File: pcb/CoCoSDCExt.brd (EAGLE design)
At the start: 101.6 x 47.3 mm, 59 parts, among them IC1 AM29F040J, IC10 YAC512-M, IC14 TL974, IC15 TL974, IC2 XC9572XLVQG64, IC3 AS6C4008SIN, IC4 SN76489R, IC5 16MHz, IC6 16MHz, IC9 YMF262-M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

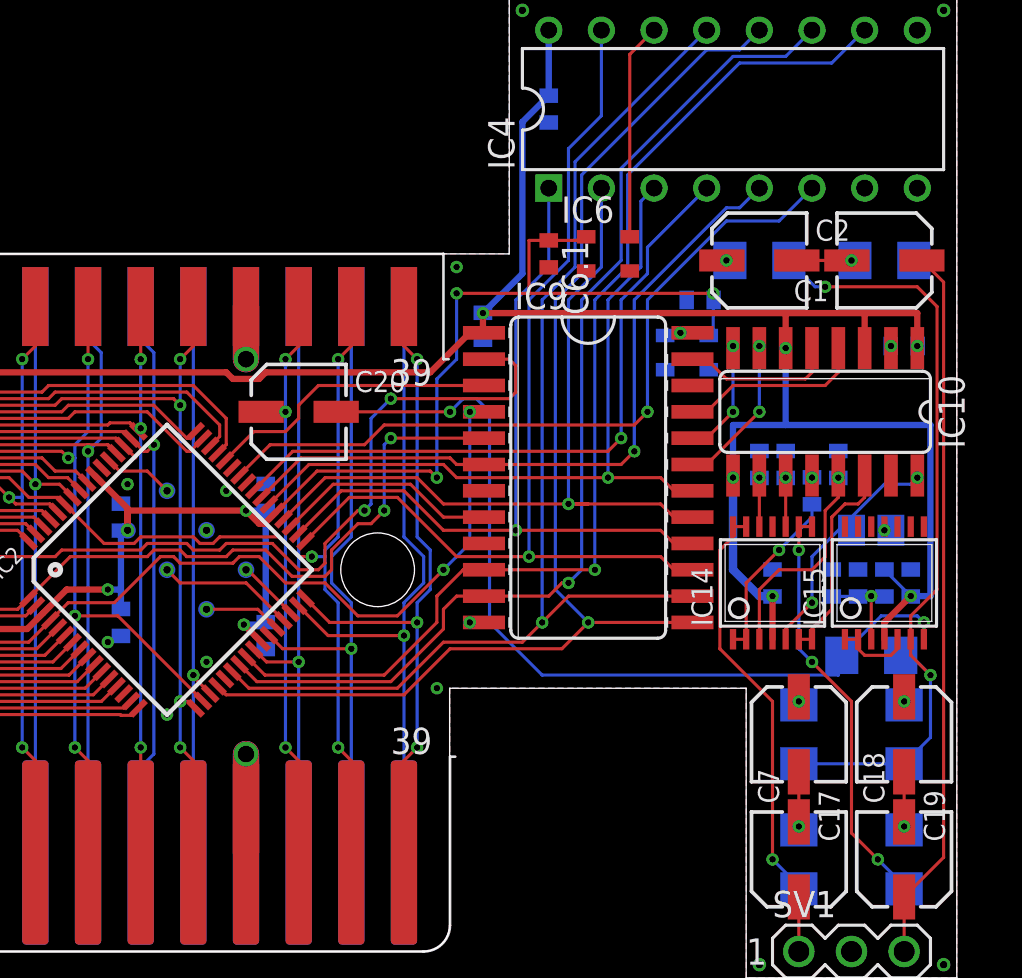
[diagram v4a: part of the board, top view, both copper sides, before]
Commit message: Fixed SN signalling
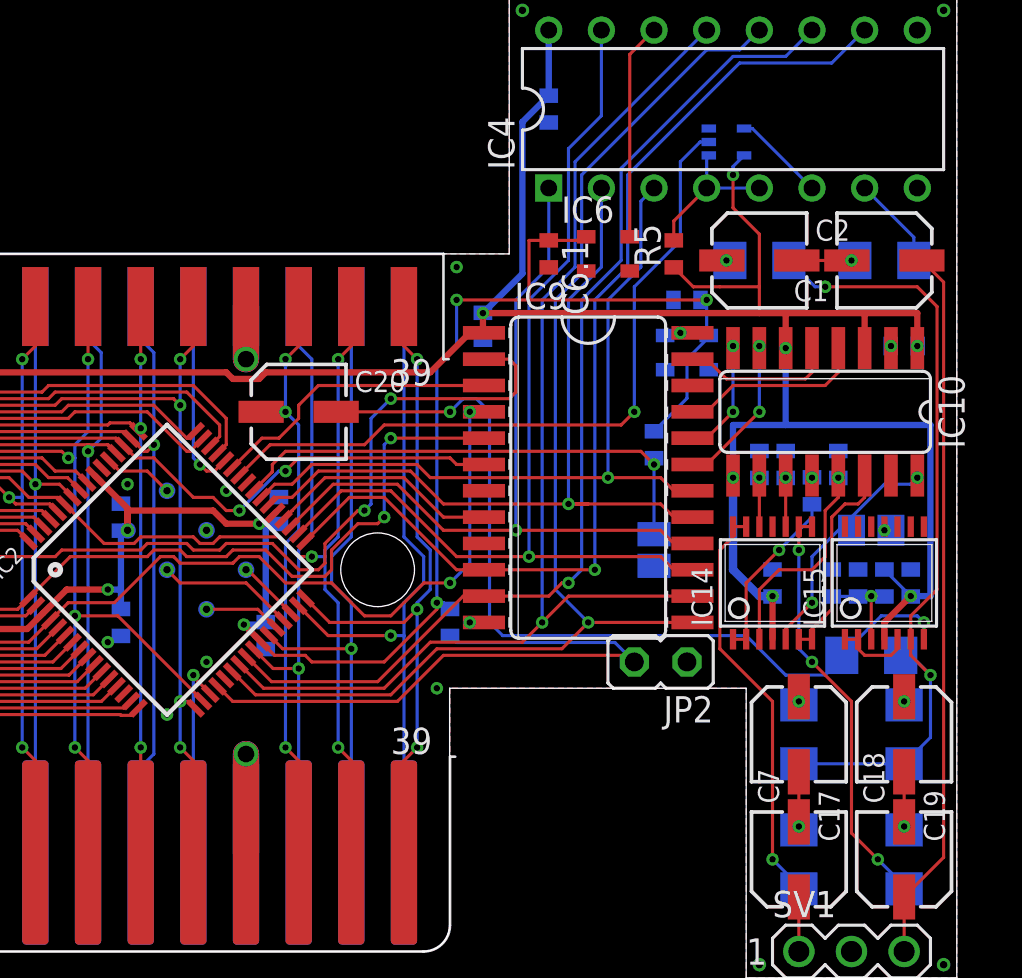
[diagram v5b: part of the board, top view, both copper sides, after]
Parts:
- added IC7: 74AHC1G08DCK, 74xx-little-us:SC70-5
- added JP2: (no value), jumper-jlb:JP1
- added R3, R4: 10K, resistor:R0402
- added R5: 2K2, resistor:R0402
- added SJ1: (no value), jumper:SJ
- IC5: value 16MHz -> 14.318MHz
- IC6: value 16MHz -> 4MHz
- moved C2.4 0.90 mm to (18.1, 21.3)
- moved C5.1 0.63 mm to (37.8, 31.4)
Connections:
- removed net !WE_AUDIO: IC2.39, IC4.5, IC9.6
- new net !CE_SN': IC4.6, IC7.4
- new net !CTS': IC2.44, X2.32
- new net N$5: IC2.40, R4.2, SJ1.2
- net !CE_SN: now also IC7.2; no longer IC4.6
- net !CE_YMF262: now also IC2.36; no longer IC2.35
- net !CTS: no longer X2.32
- net !RESET_AUDIO: now also IC2.43; no longer IC2.44
- net !WE: now also IC9.6
- net +3V3: now also R3.1, R4.1
- net +5V: now also IC7.5, R5.1
- net DB0: now also IC2.33; no longer IC2.24
- net DB1: now also IC2.24; no longer IC2.23
- net DB2: now also IC2.22; no longer IC2.20
- net DB3: now also IC2.23; no longer IC2.22
- net DB4: now also IC2.34; no longer IC2.33
- net DB5: now also IC2.35; no longer IC2.34
- net DB6: now also IC2.38; no longer IC2.36
- net DB7: now also IC2.39; no longer IC2.38
- net GND: now also IC7.3, JP2.1, SJ1.1
- net N$4: now also IC2.20, JP2.2, R3.2; no longer IC2.43
- net READY: now also IC4.5, IC7.1, R5.2; no longer IC2.40
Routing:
- net !WE_AUDIO: track 34.7 -> 0.00 mm, vias 1 -> 0
- net N$4: track 0.00 -> 30.9 mm
- net READY: track 32.5 -> 7.34 mm, vias 1 -> 0
- net N$5: track 0.00 -> 24.2 mm, vias 0 -> 1
- net !WE: track 64.0 -> 83.1 mm, vias 0 -> 2
- net !CTS: track 27.6 -> 9.79 mm
- net +3V3: track 130.6 -> 144.1 mm
- net +5V: track 237.7 -> 250.5 mm, vias 13 -> 14
- net !CTS': track 0.00 -> 9.30 mm, vias 0 -> 1
- net SN_CH_0: track 0.00 -> 4.48 mm
- net !CE_SN': track 0.00 -> 4.47 mm
- net DB0: track 54.0 -> 50.3 mm
- net !CE_SN: track 36.5 -> 35.1 mm
- net DB1: track 51.8 -> 51.0 mm
- net DB6: track 38.2 -> 38.9 mm
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
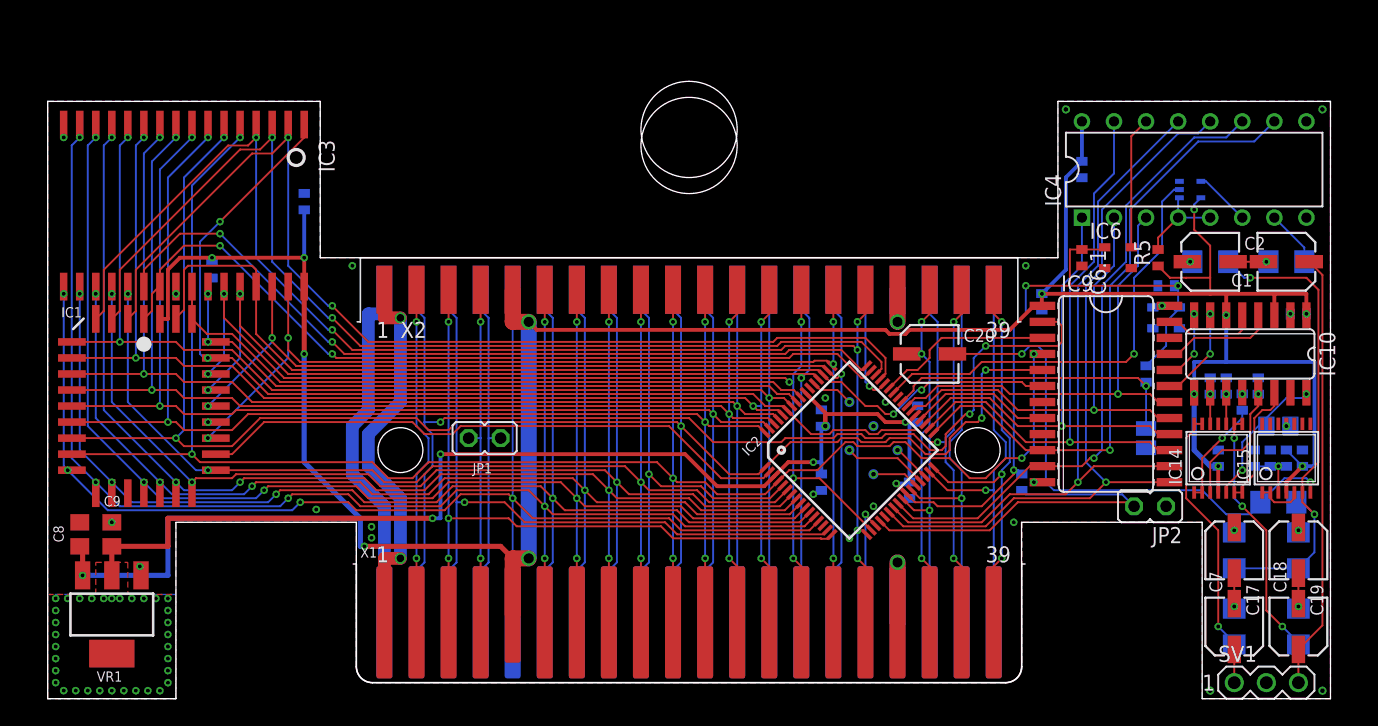
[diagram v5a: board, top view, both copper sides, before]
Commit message: Optimized SN signalling and reduced parts count
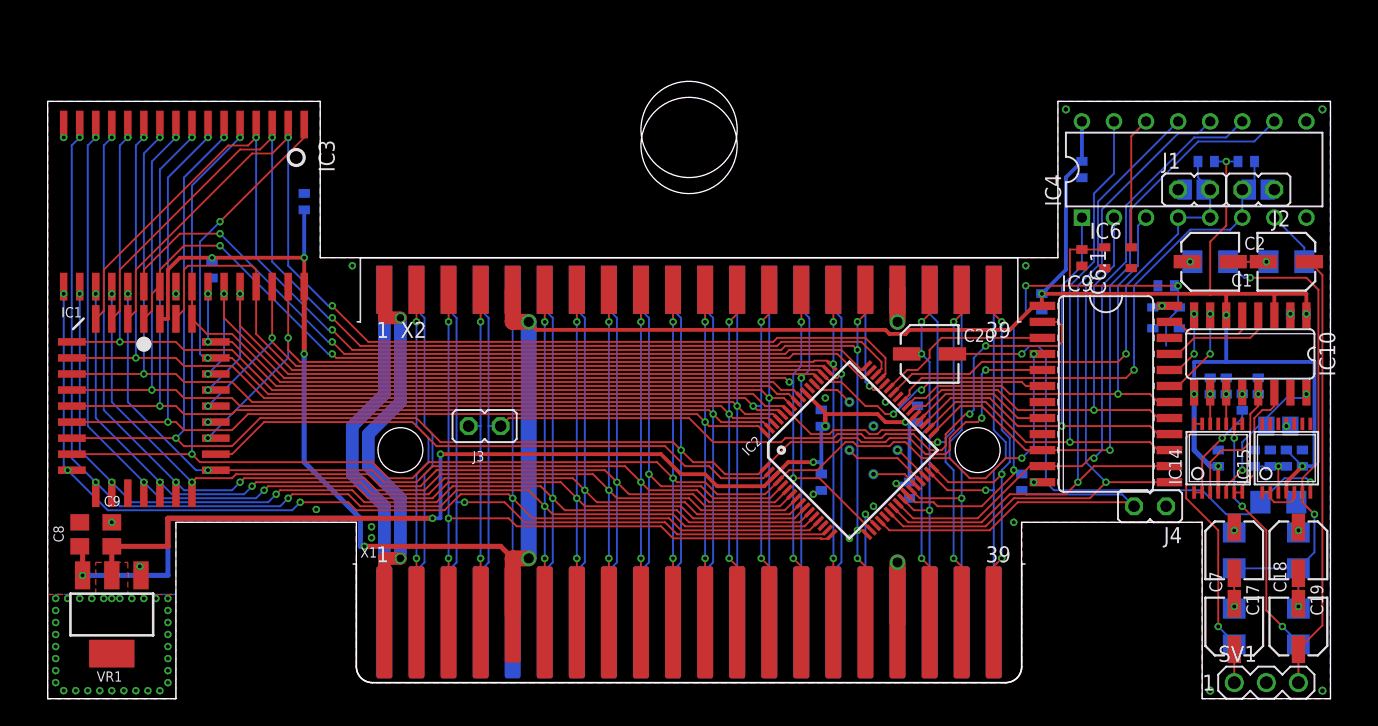
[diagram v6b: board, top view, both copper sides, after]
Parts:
- removed IC7: 74AHC1G08DCK, 74xx-little-us:SC70-5
- removed JP1: (no value), jumper-jlb:JP1
- added J1, J2, J3: (no value), jumper-jlb:JP1
- added SJ2: (no value), jumper:SJ
- R3: value 10K -> 2K2
- R5: value 2K2 -> 10K
- moved R3 29.3 mm to (41.0, 41.3), turned to 0 degrees
- moved SJ1 20.1 mm to (40.0, 39.1), turned to 180 degrees
- moved R4 13.1 mm to (26.4, 15.9)
- moved R5 10.3 mm to (44.1, 41.3), flipped to the bottom, turned to 180 degrees
- renumbered JP2 to J4
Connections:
- removed net !CE_SN': IC4.6, IC7.4
- removed net N$4: IC2.20, J4.2, R3.2
- removed net N$5: IC2.40, R4.2, SJ1.2
- new net !ROM_EN: IC2.20, J4.2, R4.2
- net !CART: now also IC9.2, J3.2; no longer JP1.2
- net !CE_SN: now also IC2.40, IC4.6, J2.2, R5.2, SJ2.2; no longer IC2.42, IC7.2
- net !NMI: no longer IC9.2
- net +3V3: no longer R3.1
- net +5V: now also R3.1; no longer IC7.5
- net GND: now also J1.1, J2.1, SJ2.1; no longer IC7.3
- net Q: now also J3.1; no longer JP1.1
- net READY: now also IC2.42, J1.2, R3.2, SJ1.2; no longer IC7.1, R5.2
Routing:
- net !NMI: track 89.3 -> 27.4 mm, vias 3 -> 0
- net !CART: track 27.8 -> 83.8 mm, vias 0 -> 2
- net READY: track 7.34 -> 40.1 mm, vias 0 -> 1
- net N$4: track 30.9 -> 0.00 mm
- net !ROM_EN: track 0.00 -> 30.9 mm
- net N$5: track 24.2 -> 0.00 mm, vias 1 -> 0
- net !CE_SN: track 35.1 -> 42.2 mm
- net !CE_SN': track 4.47 -> 0.00 mm
- net +3V3: track 144.1 -> 141.9 mm
- net +12V: track 29.2 -> 28.4 mm
- net !CE_FLASH: track 47.5 -> 46.9 mm
- net A1: track 141.0 -> 140.5 mm
